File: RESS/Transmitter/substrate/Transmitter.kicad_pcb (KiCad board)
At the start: 2 copper layers, 50 x 46 mm, 13 parts, among them J3 ADP_L, J4 ADP_R, U1 SeeeduinoXIAO

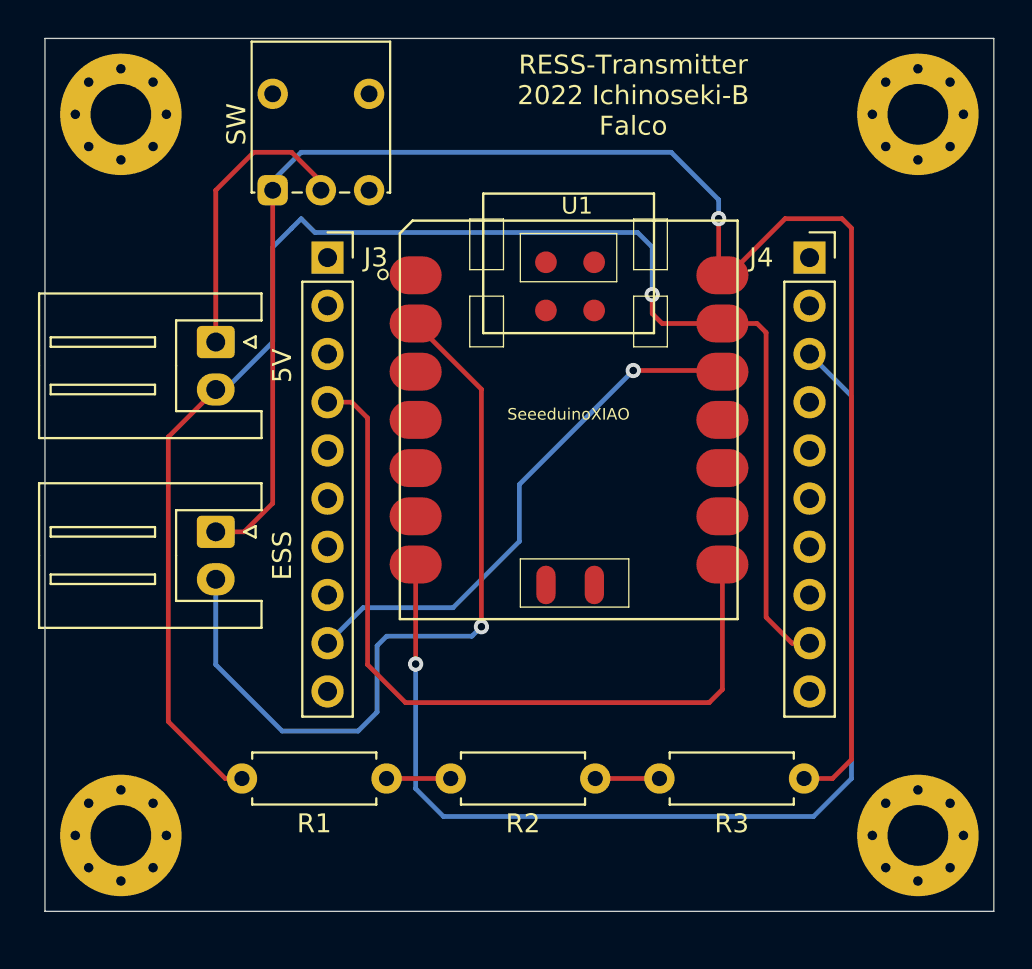
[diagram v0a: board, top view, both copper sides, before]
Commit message: 送信基板の追加とファイルの整理
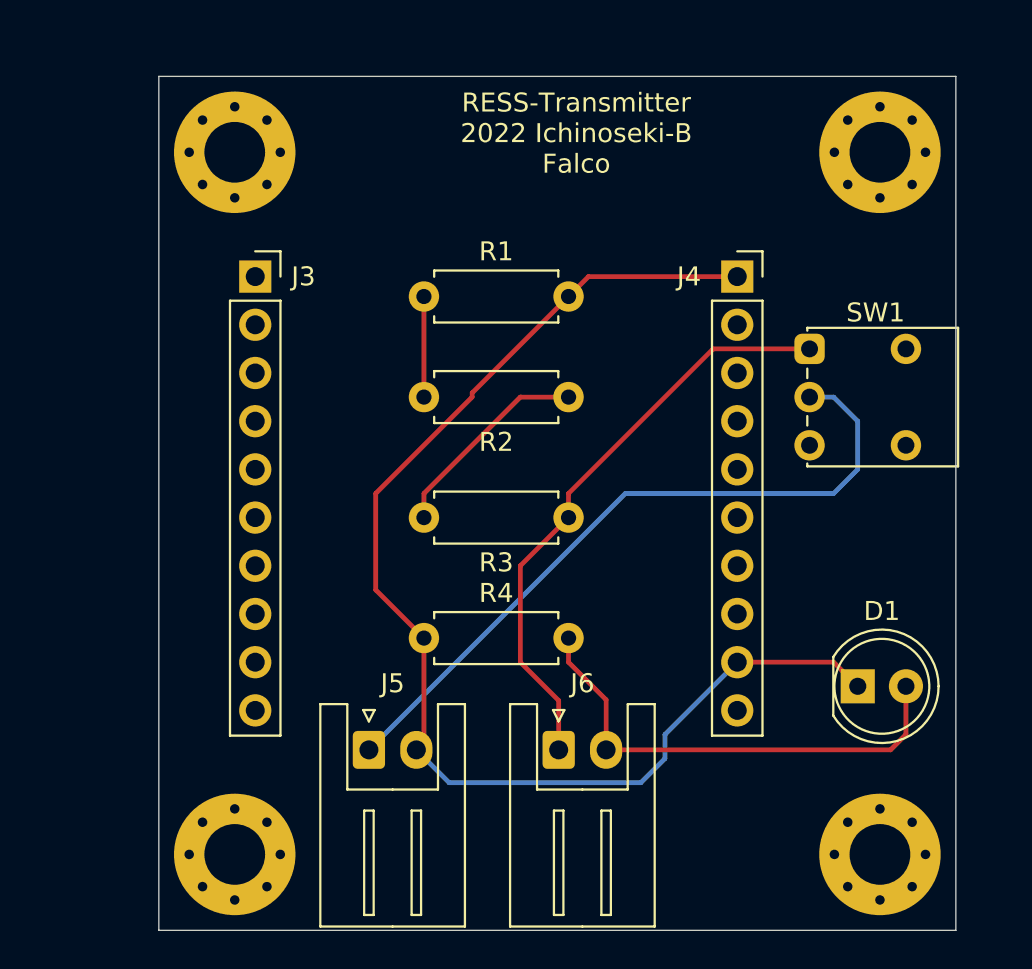
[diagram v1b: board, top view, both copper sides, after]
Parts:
- removed REF** (x4): MountingHole_3.2mm_M3_Pad_Via, MountingHole:MountingHole_3.2mm_M3_Pad_Via
- removed U1: SeeeduinoXIAO, Seeeduino XIAO KICAD:Seeeduino XIAO-MOUDLE14P-2.54-21X17.8MM
- added D1: LED, LED_THT:LED_D5.0mm, F.Cu at (163.8, 104.1)
- added H1: MountingHole, MountingHole:MountingHole_3.2mm_M3_Pad_Via, F.Cu at (131.0, 76.0)
- added H2: MountingHole, MountingHole:MountingHole_3.2mm_M3_Pad_Via, F.Cu at (131.0, 113.0)
- added H3: MountingHole, MountingHole:MountingHole_3.2mm_M3_Pad_Via, F.Cu at (165.0, 113.0)
- added H4: MountingHole, MountingHole:MountingHole_3.2mm_M3_Pad_Via, F.Cu at (165.0, 76.0)
- added R4: 10kΩ, Resistor_THT:R_Axial_DIN0207_L6.3mm_D2.5mm_P7.62mm_Horizontal, F.Cu at (141.0, 101.6)
- moved SW1 29.5 mm to (161.3, 86.4), turned to 0 degrees
- moved R1 25.5 mm to (141.0, 83.6), turned to 0 degrees
- moved J5 23.0 mm to (138.1, 107.5), turned to 0 degrees
- moved J6 21.4 mm to (148.1, 107.5), turned to 0 degrees
- moved R2 20.1 mm to (148.6, 88.9)
- moved R3 18.5 mm to (148.6, 95.2)
- moved J4 3.94 mm to (157.5, 82.5)
- moved J3 3.94 mm to (132.1, 82.5)
- renumbered 5V to J5, ESS to J6, SW to SW1
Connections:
- J3 pad 4: RX -> (no net)
- J3 pad 5: (no net) -> +3V3
- J4 pad 1: (no net) -> ESS
- J4 pad 3: TX -> (no net)
- J4 pad 9: GND -> ESS
- J5 pad 2: GND -> ESS
- J6 pad 2: ESS_IN -> LED
- R1 pad 2: GND -> ESS
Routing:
- net GND: track 81.7 -> 0.00 mm, vias 1 -> 0
- net ESS: track 0.00 -> 66.5 mm
- net TX: track 59.5 -> 0.00 mm, vias 1 -> 0
- net +5V: track 89.0 -> 31.3 mm, vias 1 -> 0
- net RX: track 41.8 -> 0.00 mm
- net ESS_IN: track 41.7 -> 0.00 mm, vias 1 -> 0
- net +3V3: track 28.5 -> 0.00 mm, vias 1 -> 0
- net LED: track 0.00 -> 25.4 mm
- net PW_IN: track 15.5 -> 37.5 mm
- net Net-(R2-Pad1): track 3.38 -> 11.0 mm
- net Net-(R1-Pad1): track 3.38 -> 5.30 mm
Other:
- board size 50 x 46 mm -> 42 x 45 mm
- board text added: "JLCJLCJLCJLC"

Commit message: 回路の細かな修正
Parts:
- added U1: TA48033S, Package_TO_SOT_THT:TO-220-3_Horizontal_TabDown, F.Cu at (141.0, 102.4)
- moved R4 22.7 mm to (161.3, 91.4), turned to 270 degrees
- moved R3 18.2 mm to (166.4, 91.4), turned to 270 degrees
- moved R2 13.7 mm to (151.8, 102.2), turned to 90 degrees
- moved R1 13.0 mm to (151.8, 90.8), turned to 90 degrees
- moved SW1 3.81 mm to (161.3, 82.5)
- moved J6 0.75 mm to (147.3, 107.5)
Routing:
- net +5V: track 31.3 -> 77.4 mm
- net +3V3: track 0.00 -> 26.6 mm
- net ESS: track 66.5 -> 82.9 mm
- net Net-(R2-Pad1): track 11.0 -> 20.3 mm
- net LED: track 25.4 -> 23.6 mm
- net Net-(R1-Pad1): track 5.30 -> 3.81 mm
- net PW_IN: track 37.5 -> 38.4 mm
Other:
- board text added: "RESS-Transmitter 2022 Ichinoseki-B"
- board text removed: "RESS-Transmitter 2022 Ichinoseki-B Falco"

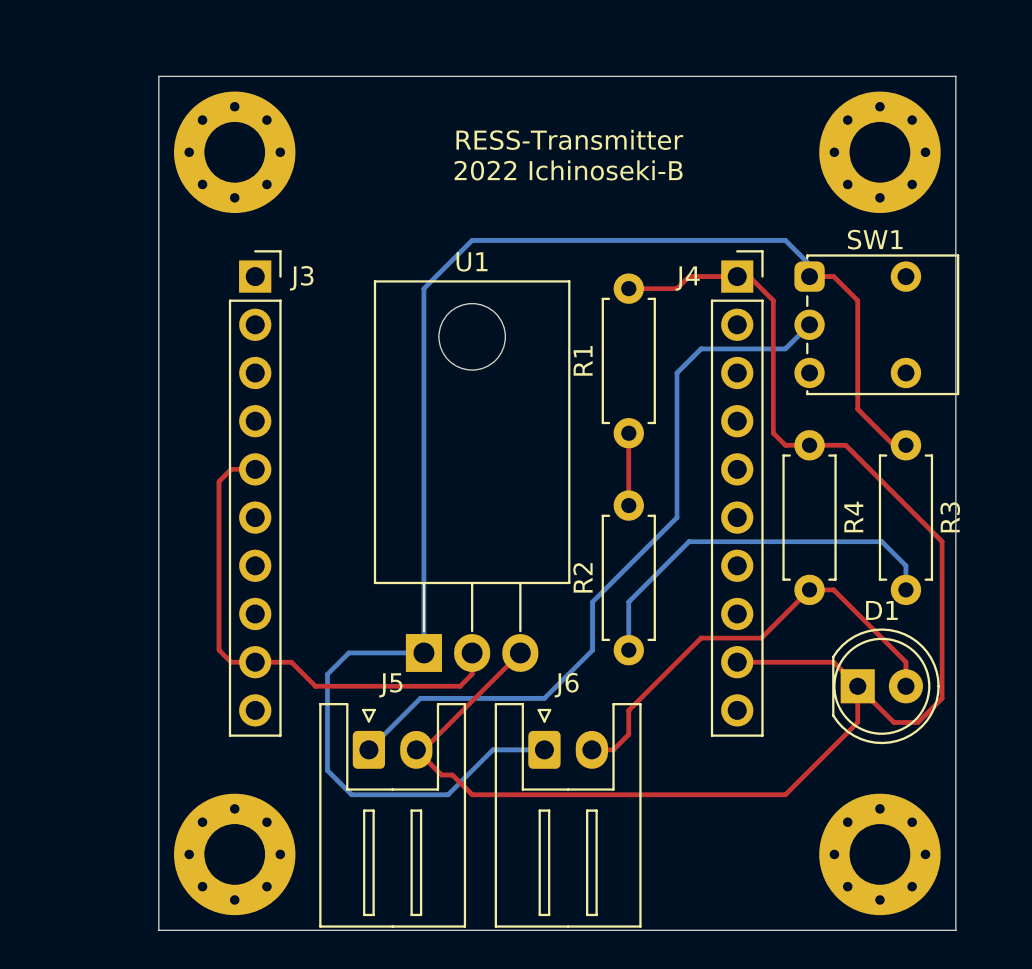
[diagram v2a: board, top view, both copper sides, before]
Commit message: 基板が燃えるほどのミスを修正
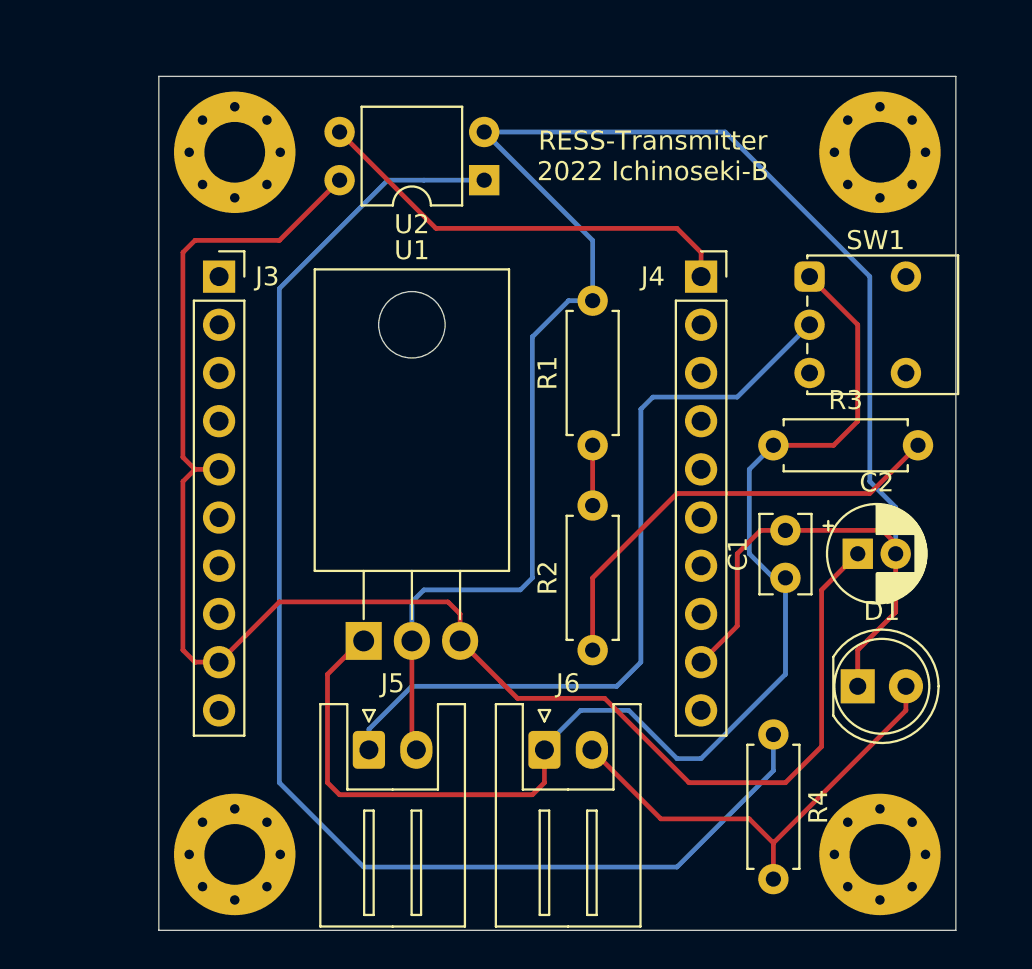
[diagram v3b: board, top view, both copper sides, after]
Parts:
- added C1: 0.33μF, Capacitor_THT:C_Rect_L4.0mm_W2.5mm_P2.50mm, F.Cu at (160.0, 98.4)
- added C2: 47μF, Capacitor_THT:CP_Radial_D5.0mm_P2.00mm, F.Cu at (163.8, 97.2)
- added U2: TLP785, Package_DIP:DIP-4_W7.62mm, F.Cu at (144.1, 77.5)
- R1, R2, R3: value 18Ω -> 22Ω
- R4: value 10kΩ -> 220Ω
- U1: value TA48033S -> BP5293
- moved R4 15.4 mm to (159.4, 106.7)
- moved R3 6.99 mm to (159.4, 91.4), turned to 0 degrees
- moved U1 3.24 mm to (137.8, 101.8)
- moved R1 2.01 mm to (149.9, 91.4)
- moved J3 1.91 mm to (130.2, 82.5)
- moved J4 1.91 mm to (155.6, 82.5)
- moved R2 1.90 mm to (149.9, 102.2)
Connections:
- D1 pad 1: ESS -> GND
- J4 pad 9: ESS -> GND
- J5 pad 2: ESS -> GND
- R1 pad 2: ESS -> GND
- R4 pad 1: ESS -> Net-(R4-Pad1)
- U1 pad 2: +3V3 -> GND
- U1 pad 3: ESS -> +3V3
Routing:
- net GND: track 0.00 -> 105.3 mm
- net Net-(R4-Pad1): track 0.00 -> 71.1 mm
- net ESS: track 82.9 -> 23.0 mm
- net +3V3: track 26.6 -> 84.3 mm
- net +5V: track 77.4 -> 66.0 mm
- net Net-(R2-Pad1): track 20.3 -> 23.8 mm
- net PW_IN: track 38.4 -> 40.9 mm
- net LED: track 23.6 -> 24.6 mm
- net Net-(R1-Pad1): track 3.81 -> 3.17 mm
